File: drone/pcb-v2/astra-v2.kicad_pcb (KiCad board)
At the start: 4 copper layers, 36 x 33.8 mm, 72 parts, among them J1 Conn_01x04_MountingPin, J2 Conn_02x08_Odd_Even, J3 Conn_01x02_Pin, M1 Motor_DC, M2 Motor_DC, M3 Motor_DC, M4 Motor_DC, Q1 AO3400A, Q2 AO3400A, Q3 AO3400A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

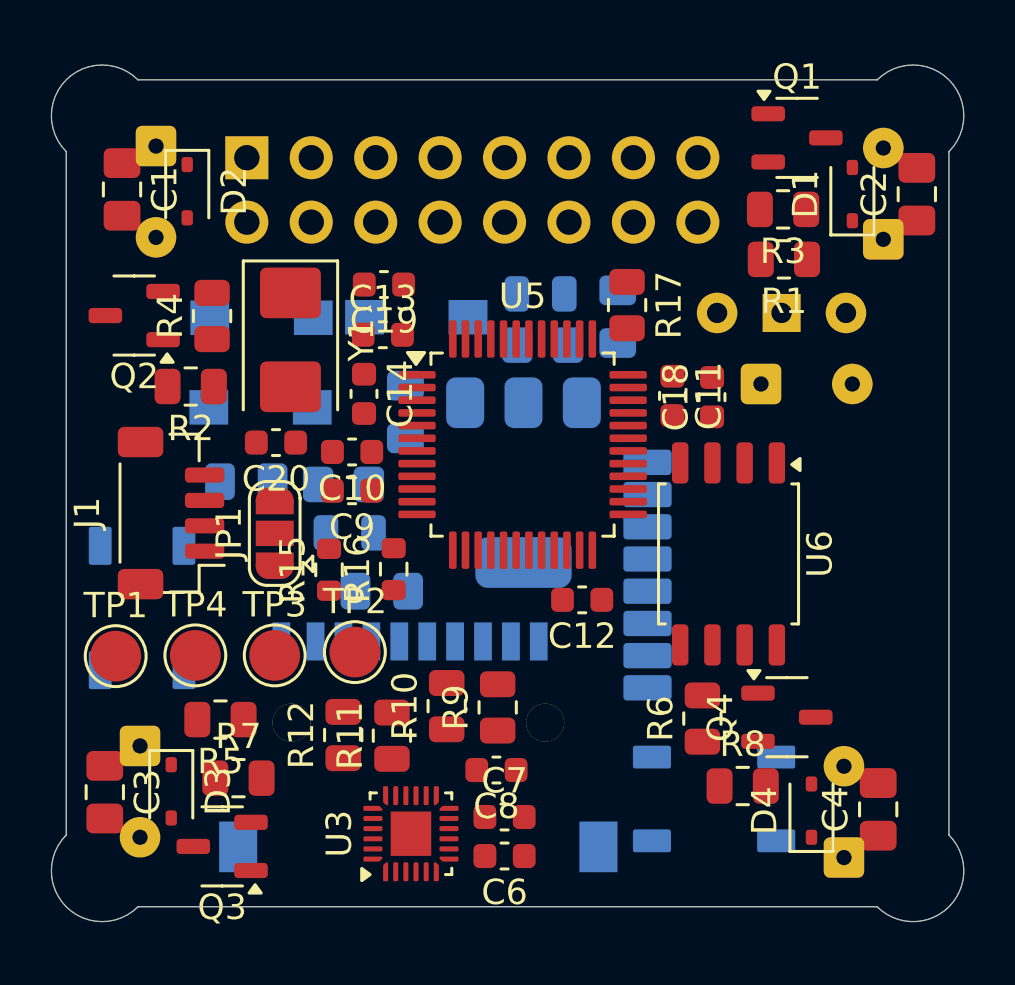
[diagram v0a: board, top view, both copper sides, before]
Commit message: [pcb] finish routing
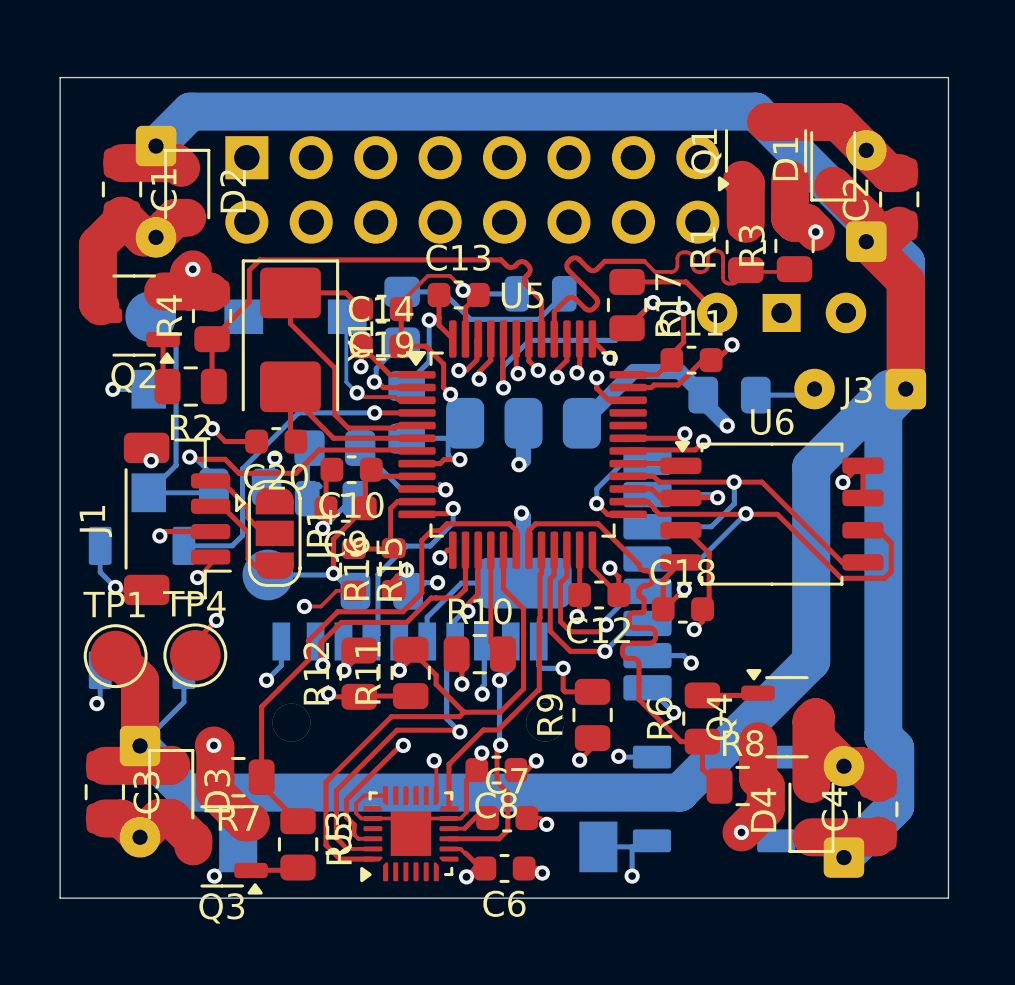
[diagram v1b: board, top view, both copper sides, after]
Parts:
- removed SW2: SW_Push, lcsc:SW-SMD_L4.0-W2.9-LS5.0
- J3: moved to F.Cu
- TP2, TP3: moved to B.Cu
- moved TP3 14.2 mm to (43.0, 69.1), turned to 180 degrees
- moved C18 8.44 mm to (64.0, 80.6), turned to 0 degrees
- moved R5 5.79 mm to (48.8, 89.9), turned to -90 degrees
- moved J3 5.71 mm to (72.8, 71.9), turned to 180 degrees
- moved R14 5.65 mm to (52.9, 69.1), turned to -90 degrees
- moved C15 5.39 mm to (65.8, 72.2), turned to 180 degrees
- moved SW3 4.61 mm to (42.9, 74.0), turned to -90 degrees
- moved TP2 4.58 mm to (47.6, 79.2), turned to 180 degrees
- moved R9 3.75 mm to (60.4, 84.8)
- moved C13 3.38 mm to (55.1, 68.2)
- moved R11 2.58 mm to (53.2, 83.1)
- moved R12 2.50 mm to (51.2, 83.1)
- moved R10 2.43 mm to (56.0, 82.4), turned to 0 degrees
- moved U6 2.32 mm to (67.5, 76.8), turned to 0 degrees
- moved C14 2.00 mm to (52.1, 70.2), turned to 0 degrees
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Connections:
- net USB_DM renamed D-
- net USB_DP renamed D+
- J2 pad 10: TCK -> TMS
- J2 pad 9: TMS -> TCK
- U1 pad 5: SPI1_CLK -> SPI2_CLK
- U1 pad 6: SPI1_MOSI -> SPI2_MOSI
- U1 pad 7: SPI1_MISO -> SPI2_MISO
- U2 pad 9: SD_CS -> SD_CD
- U5 pad 10: BAT_MEASURE -> STATUS_LED_1
- U5 pad 11: NEOPIXEL -> BAT_MEASURE
- U5 pad 12: STATUS_LED_1 -> SD_CS
- U5 pad 13: SD_CD -> IMU_CS
- U5 pad 14: SD_CS -> SD_CD
- U5 pad 20: NRF_CS -> IMU_INT1
- U5 pad 22: NRF_IRQ -> NRF_CS
- U5 pad 25: IMU_INT1 -> NRF_IRQ
- U5 pad 4: BTN2 -> NEOPIXEL
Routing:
- net +BATT: track 0.00 -> 161.9 mm, vias 0 -> 3
- net GND: track 0.00 -> 91.8 mm, vias 0 -> 28
- net +3.3V: track 0.00 -> 55.8 mm, vias 0 -> 16
- net Net-(D5-DOUT): track 0.00 -> 26.7 mm, vias 0 -> 2
- net SPI1_MOSI: track 0.00 -> 25.1 mm, vias 0 -> 1
- net RST: track 0.00 -> 22.0 mm, vias 0 -> 1
- net MOTOR3: track 0.00 -> 20.8 mm
- net MOTOR4: track 0.00 -> 19.9 mm
- net MOTOR2: track 0.00 -> 19.9 mm
- net SPI2_CLK: track 0.00 -> 18.8 mm, vias 0 -> 1
- net MOTOR1: track 0.00 -> 17.9 mm
- net SPI1_CLK: track 0.00 -> 17.6 mm, vias 0 -> 2
- net SPI1_MISO: track 0.00 -> 15.7 mm, vias 0 -> 2
- net IMU_CS: track 0.00 -> 15.7 mm, vias 0 -> 2
- net UART1_TX: track 0.00 -> 15.5 mm, vias 0 -> 1
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- added copper zone on In2.Cu, net +3.3V
- added copper zone on In1.Cu, net GND
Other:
- board size 36 x 33.8 mm -> 35 x 32.3 mm

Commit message: [pcb] drc fixes
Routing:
- net D-: track 0.06 -> 13.9 mm, vias 0 -> 1
- net D+: track 6.93 -> 13.8 mm, vias 0 -> 1
